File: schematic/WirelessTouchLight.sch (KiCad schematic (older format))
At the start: 10 parts, among them J1 Conn_01x04, J2 HLK-PM03, K1 HK4100F-DC3V-SHG, Q1 2N2222, U1 WeMos_mini

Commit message: Update schematic
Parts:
- J1: footprint Terminal_Blocks:TerminalBlock_bornier-4_P5.08mm -> KF-TerminalBlock:KF235-4P
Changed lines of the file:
@@
 EESchema Schematic File Version 4
+LIBS:WirelessTouchLight-cache
 EELAYER 30 0
 EELAYER END
@@
 F 0 "J1" H 918 1817 50  0000 C CNN
 F 1 "Conn_01x04" H 918 1726 50  0000 C CNN
-F 2 "Terminal_Blocks:TerminalBlock_bornier-4_P5.08mm" H 1000 1500 50  0001 C CNN
+F 2 "KF-TerminalBlock:KF235-4P" H 1000 1500 50  0001 C CNN
 F 3 "~" H 1000 1500 50  0001 C CNN
 	1    1000 1500

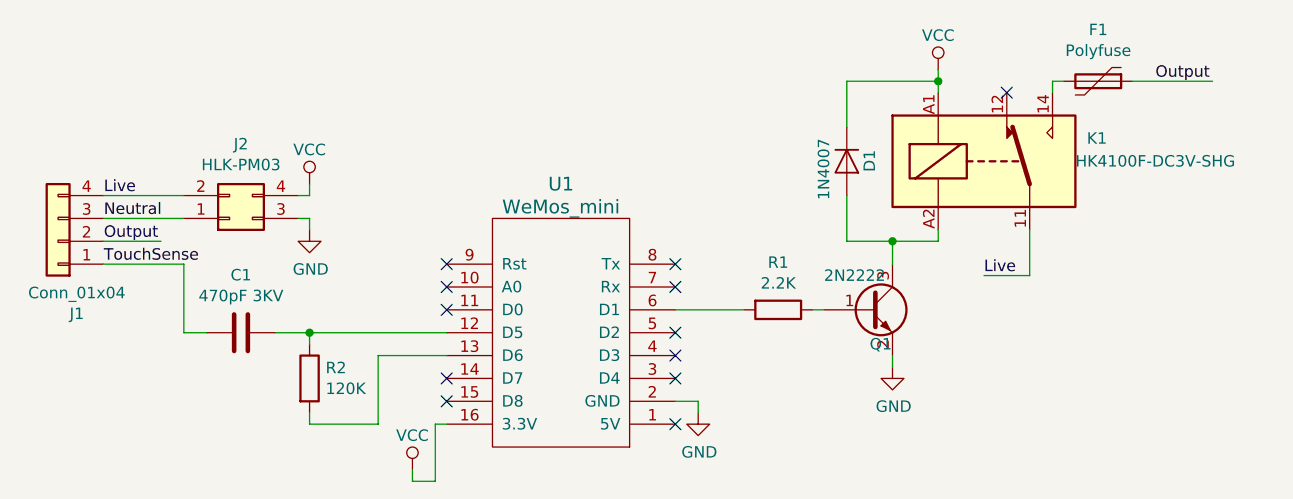
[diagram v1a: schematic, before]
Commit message: Change to 470K Resistor
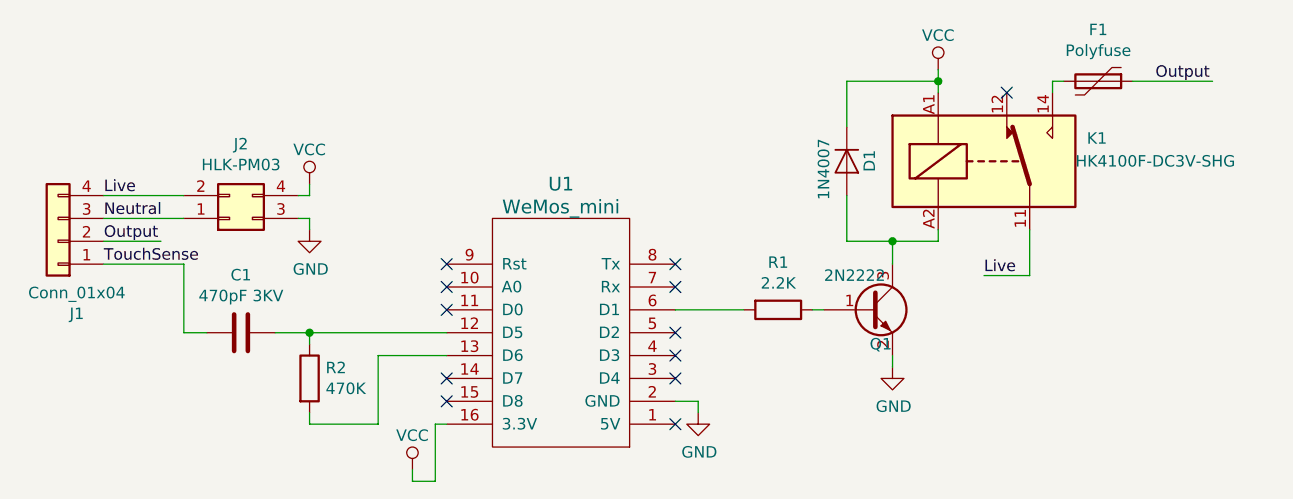
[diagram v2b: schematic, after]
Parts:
- R2: value 120K -> 470K
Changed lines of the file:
@@
 P 2100 2100
 F 0 "R2" H 2170 2146 50  0000 L CNN
-F 1 "120K" H 2170 2055 50  0000 L CNN
+F 1 "470K" H 2170 2055 50  0000 L CNN
 F 2 "Resistors_SMD:R_0805_HandSoldering" V 2030 2100 50  0001 C CNN
 F 3 "~" H 2100 2100 50  0001 C CNN

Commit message: Change Back to 100K resistor (470 too much noises)
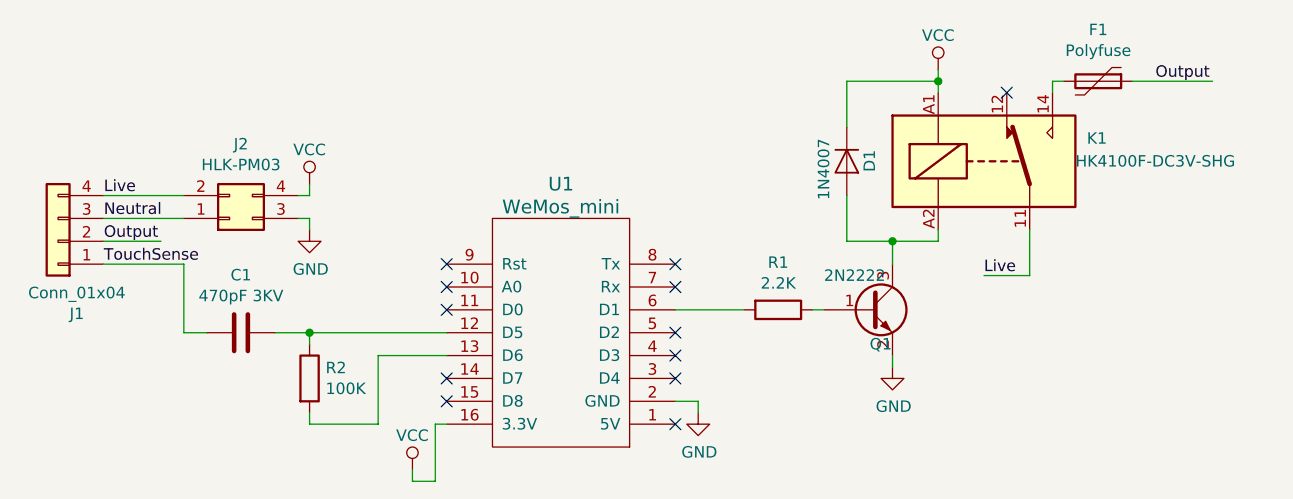
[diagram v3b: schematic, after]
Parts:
- R2: value 470K -> 100K
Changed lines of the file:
@@
 P 2100 2100
 F 0 "R2" H 2170 2146 50  0000 L CNN
-F 1 "470K" H 2170 2055 50  0000 L CNN
+F 1 "100K" H 2170 2055 50  0000 L CNN
 F 2 "Resistors_SMD:R_0805_HandSoldering" V 2030 2100 50  0001 C CNN
 F 3 "~" H 2100 2100 50  0001 C CNN

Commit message: Update schematic/PCB
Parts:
- F1: value Polyfuse -> TRF250-1000
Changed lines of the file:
@@
 EESchema Schematic File Version 4
-LIBS:WirelessTouchLight-cache
 EELAYER 30 0
 EELAYER END
@@
 P 5550 800
 F 0 "F1" V 5325 800 50  0000 C CNN
-F 1 "Polyfuse" V 5416 800 50  0000 C CNN
+F 1 "TRF250-1000" V 5416 800 50  0000 C CNN
 F 2 "fuse:TRF250-1000" H 5600 600 50  0001 L CNN
 F 3 "~" H 5550 800 50  0001 C CNN
